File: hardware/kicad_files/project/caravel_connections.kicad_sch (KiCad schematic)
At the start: 13 parts, among them J1 Conn_01x03_Pin, J2 Conn_01x03_Pin, J3 Conn_01x03_Pin, U2 C2977809

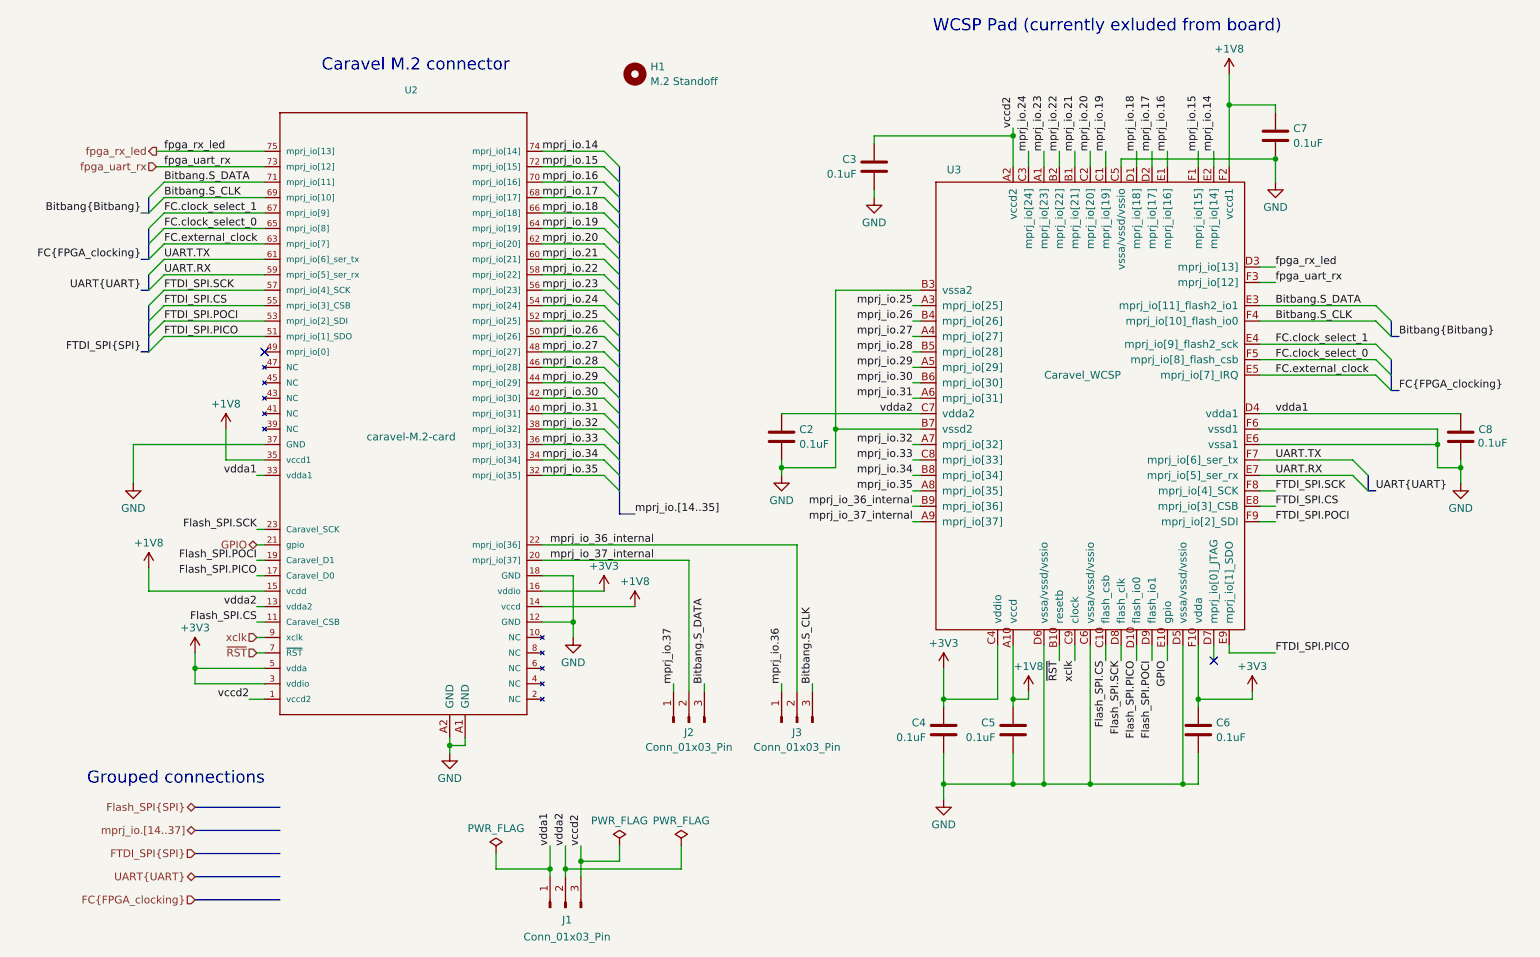
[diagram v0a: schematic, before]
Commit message: feat: update to 0.2
feat: add pin sockets compatible to the Pmod interface

feat: add a power switch and an overcurrent protection circuit, including a fault status LED and a solder bridge

fix: remove the clock jumpers and directly connect the second output clock to the user clock input

misc: remove the jumpers from io 36 and 37 to the bitbang inputs, add bitbang pins to the UART connector

cosmetic: make the PCB edges round
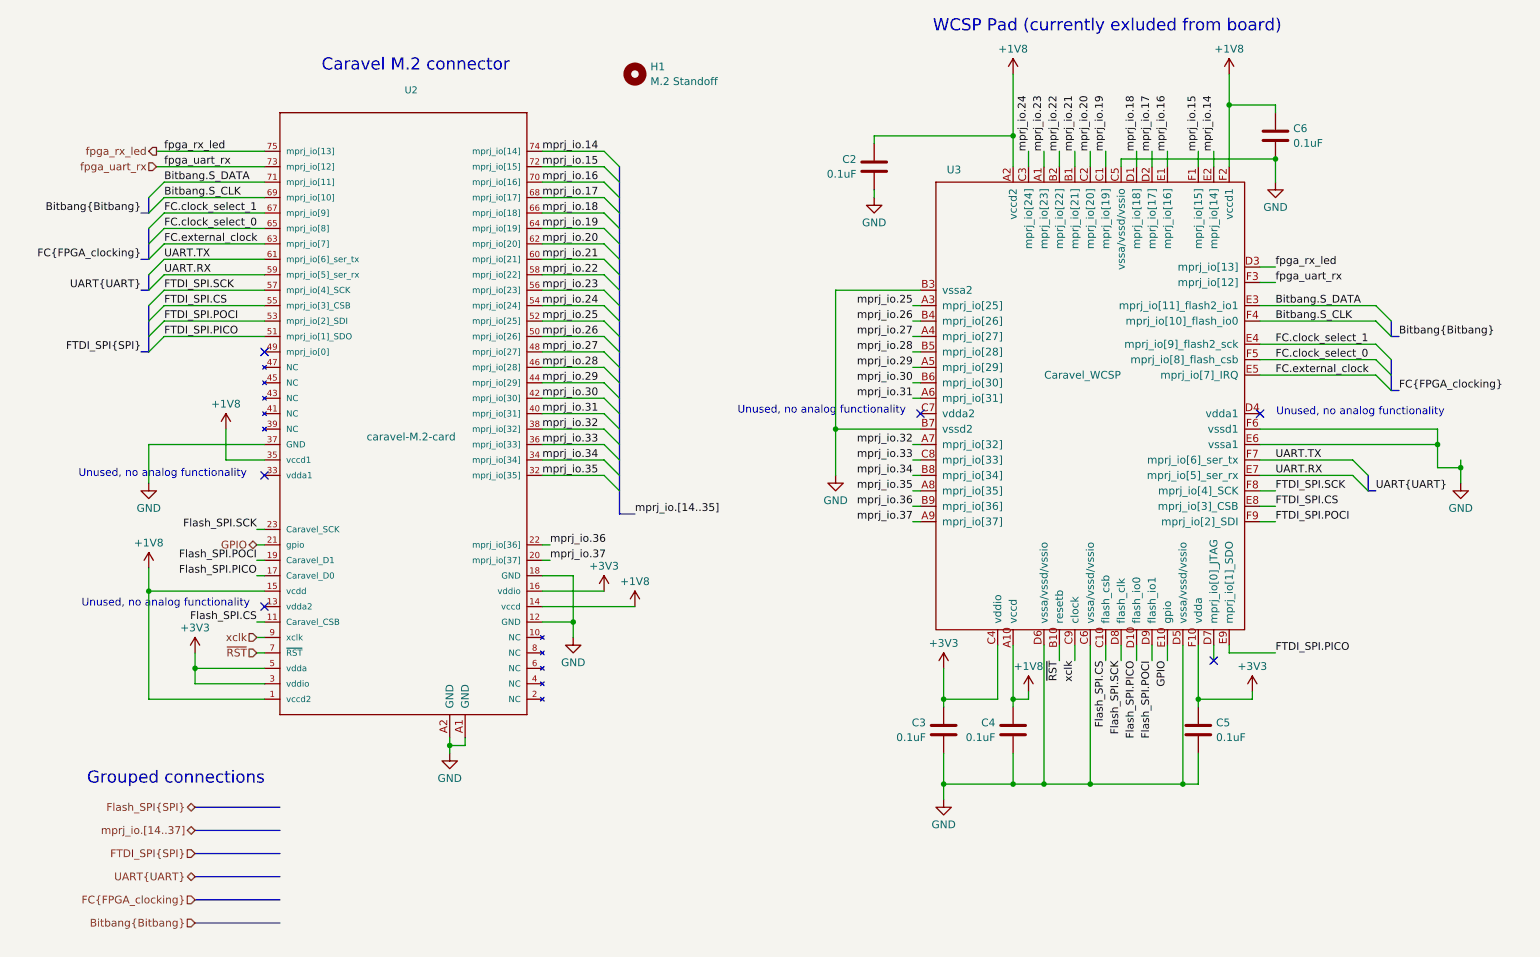
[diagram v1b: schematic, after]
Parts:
- removed C2, C8: 0.1uF, Capacitor_SMD:C_0402_1005Metric, symbol Device:C
- removed J1, J2, J3: Conn_01x03_Pin, Connector_PinHeader_2.54mm:PinHeader_1x03_P2.54mm_Vertical, symbol Connector:Conn_01x03_Pin
- renumbered C3 to C2, C4 to C3, C5 to C4, C6 to C5, C7 to C6
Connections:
- net mprj_io_36_internal is gone; now on net mprj_io.36: U2.22 (mprj_io[36]), U3.B9 (mprj_io[36])
- net mprj_io_37_internal is gone; now on net mprj_io.37: U2.20 (mprj_io[37]), U3.A9 (mprj_io[37])
- net vccd2 is gone; now on net +1V8: C2.1, U2.1 (vccd2), U3.A2 (vccd2)
- net vdda1: no longer names the net of U3.D4 (vdda1)
- net vdda1: no longer U2.33 (vdda1)
- net vdda2: no longer names the net of U3.C7 (vdda2)
- net vdda2: no longer U2.13 (vdda2)
- no-connect marks 2 -> 6
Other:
- note added: "Unused, no analog functionality"
